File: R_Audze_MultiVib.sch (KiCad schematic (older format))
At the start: 11 parts

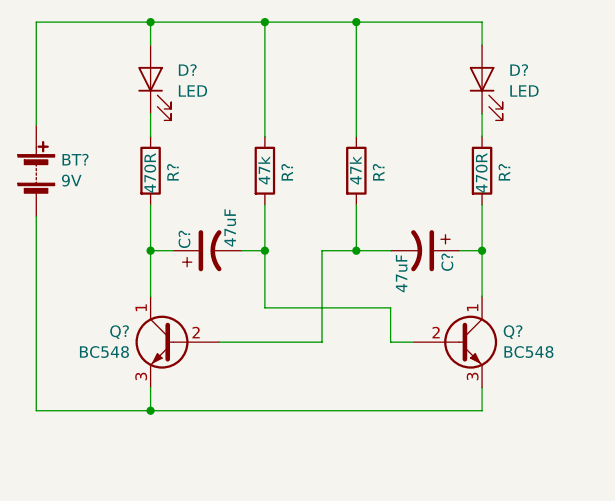
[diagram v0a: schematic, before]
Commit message: Replaced transistors with a double unit IC
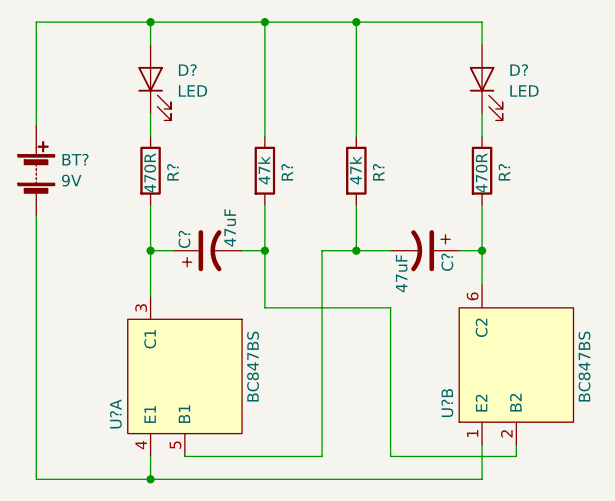
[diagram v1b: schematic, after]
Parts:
- removed Q? (x2): BC548, Package_TO_SOT_THT:TO-92_Inline, symbol Transistor_BJT:BC548
- added U? (x2): BC847BS, symbol project_library:BC847BS
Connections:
- net at BT?.2 (-): now also U?.1 (E2), U?.4 (E1)
- net at C?.1, R?.2: now also U?.3 (C1)
- net at C?.2, R?.2: now also U?.2 (B2)
- net at C?.2, R?.2: now also U?.5 (B1)
- net at C?.1, R?.2: now also U?.6 (C2)
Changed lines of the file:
@@
 EESchema Schematic File Version 4
+LIBS:R_Audze_MultiVib-cache
 EELAYER 26 0
 EELAYER END
@@
 $Comp
 L Device:CP1 C?
-U 1 1 5E56251E
-P 3350 4450
-F 0 "C?" H 3400 4550 50  0000 C CNN
-F 1 "47uF" H 3450 4350 50  0000 C CNN
-F 2 "" H 3350 4450 50  0001 C CNN
-F 3 "~" H 3350 4450 50  0001 C CNN
-	1    3350 4450
-	0    -1   -1   0
-$EndComp
-$Comp
-L Device:CP1 C?
 U 1 1 5E562593
 P 4300 4450
@@
 Wire Wire Line
 	4550 3450 4550 3550
-Connection ~ 3600 3450
 Wire Wire Line
 	4550 3950 4550 3850
@@
 Wire Wire Line
 	4000 3450 4550 3450
-$Comp
-L Transistor_BJT:BC548 Q?
-U 1 1 5E562A15
-P 3200 4850
-F 0 "Q?" H 3390 4896 50  0000 L CNN
-F 1 "BC548" H 3390 4805 50  0000 L CNN
-F 2 "Package_TO_SOT_THT:TO-92_Inline" H 3400 4775 50  0001 L CIN
-F 3 "http://www.fairchildsemi.com/ds/BC/BC547.pdf" H 3200 4850 50  0001 L CNN
-	1    3200 4850
-	-1   0    0    -1
-$EndComp
-$Comp
-L Transistor_BJT:BC548 Q?
-U 1 1 5E562A81
-P 4450 4850
-F 0 "Q?" H 4641 4896 50  0000 L CNN
-F 1 "BC548" H 4641 4805 50  0000 L CNN
-F 2 "Package_TO_SOT_THT:TO-92_Inline" H 4650 4775 50  0001 L CIN
-F 3 "http://www.fairchildsemi.com/ds/BC/BC547.pdf" H 4450 4850 50  0001 L CNN
-	1    4450 4850
-	1    0    0    -1
-$EndComp
 Wire Wire Line
 	3100 4450 3100 4650
@@
 Wire Wire Line
 	4000 4450 3850 4450
-Wire Wire Line
-	3850 4450 3850 4850
-Wire Wire Line
-	3850 4850 3400 4850
 Connection ~ 4000 4450
 Wire Wire Line
@@
 Wire Wire Line
 	3600 4700 4150 4700
-Wire Wire Line
-	4150 4700 4150 4850
-Wire Wire Line
-	4150 4850 4250 4850
 Connection ~ 3600 4450
 Wire Wire Line
-	4550 4450 4550 4650
+	4550 4450 4550 4600
 Connection ~ 4550 4450
 Wire Wire Line
@@
 	2600 3450 3100 3450
 Wire Wire Line
-	2600 4300 2600 5150
-Wire Wire Line
-	2600 5150 3100 5150
-Wire Wire Line
-	4550 5150 4550 5050
-Wire Wire Line
-	3100 5050 3100 5150
-Connection ~ 3100 5150
-Wire Wire Line
-	3100 5150 4550 5150
+	2600 4300 2600 5450
+Wire Wire Line
+	2600 5450 3100 5450
+Wire Wire Line
+	4550 5450 4550 5300
+Connection ~ 3100 5450
+Wire Wire Line
+	3100 5450 4550 5450
+Connection ~ 3600 3450
+$Comp
+L Device:CP1 C?
+U 1 1 5E56251E
+P 3350 4450
+F 0 "C?" H 3400 4550 50  0000 C CNN
+F 1 "47uF" H 3450 4350 50  0000 C CNN
+F 2 "" H 3350 4450 50  0001 C CNN
+F 3 "~" H 3350 4450 50  0001 C CNN
+	1    3350 4450
+	0    -1   -1   0
+$EndComp
+$Comp
+L project_library:BC847BS U?
+U 1 1 5E5F7330
+P 3250 5000
+F 0 "U?" H 3350 4700 50  0000 L CNN
+F 1 "BC847BS" H 3050 5300 50  0000 L CNN
+F 2 "" H 3250 4900 50  0001 C CNN
+F 3 "" H 3250 4900 50  0001 C CNN
+	1    3250 5000
+	0    1    1    0
+$EndComp
+$Comp
+L project_library:BC847BS U?
+U 2 1 5E5F737F
+P 4700 4950
+F 0 "U?" H 4600 5250 50  0000 R CNN
+F 1 "BC847BS" H 4850 4650 50  0000 R CNN
+F 2 "" H 4700 4850 50  0001 C CNN
+F 3 "" H 4700 4850 50  0001 C CNN
+	2    4700 4950
+	0    -1   -1   0
+$EndComp
+Wire Wire Line
+	3850 5350 3250 5350
+Wire Wire Line
+	3850 4450 3850 5350
+Wire Wire Line
+	3100 5350 3100 5450
+Wire Wire Line
+	4150 5350 4700 5350
+Wire Wire Line
+	4700 5350 4700 5300
+Wire Wire Line
+	4150 4700 4150 5350
 $EndSCHEMATC

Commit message: Added component annotations
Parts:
- gave numbers to parts that had none: 10
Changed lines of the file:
@@
 $EndDescr
 $Comp
-L Device:Battery BT?
+L Device:Battery BT1
 U 1 1 5E562185
 P 2600 4100
-F 0 "BT?" H 2708 4146 50  0000 L CNN
+F 0 "BT1" H 2708 4146 50  0000 L CNN
 F 1 "9V" H 2708 4055 50  0000 L CNN
 F 2 "" V 2600 4160 50  0001 C CNN
@@
 $EndComp
 $Comp
-L Device:LED D?
+L Device:LED D1
 U 1 1 5E56220C
 P 3100 3700
-F 0 "D?" V 3138 3583 50  0000 R CNN
+F 0 "D1" V 3138 3583 50  0000 R CNN
 F 1 "LED" V 3047 3583 50  0000 R CNN
 F 2 "" H 3100 3700 50  0001 C CNN
@@
 $EndComp
 $Comp
-L Device:LED D?
+L Device:LED D2
 U 1 1 5E56224F
 P 4550 3700
-F 0 "D?" V 4588 3583 50  0000 R CNN
+F 0 "D2" V 4588 3583 50  0000 R CNN
 F 1 "LED" V 4497 3583 50  0000 R CNN
 F 2 "" H 4550 3700 50  0001 C CNN
@@
 $EndComp
 $Comp
-L Device:R R?
+L Device:R R1
 U 1 1 5E562292
 P 3100 4100
-F 0 "R?" V 3200 4050 50  0000 L CNN
+F 0 "R1" V 3200 4050 50  0000 L CNN
 F 1 "470R" V 3100 4000 50  0000 L CNN
 F 2 "" V 3030 4100 50  0001 C CNN
@@
 $EndComp
 $Comp
-L Device:R R?
+L Device:R R2
 U 1 1 5E5622C0
 P 3600 4100
-F 0 "R?" V 3700 4050 50  0000 L CNN
+F 0 "R2" V 3700 4050 50  0000 L CNN
 F 1 "47k" V 3600 4100 50  0000 C CNN
 F 2 "" V 3530 4100 50  0001 C CNN
@@
 $EndComp
 $Comp
-L Device:R R?
+L Device:R R3
 U 1 1 5E5622F0
 P 4000 4100
-F 0 "R?" V 4100 4050 50  0000 L CNN
+F 0 "R3" V 4100 4050 50  0000 L CNN
 F 1 "47k" V 4000 4100 50  0000 C CNN
 F 2 "" V 3930 4100 50  0001 C CNN
@@
 $EndComp
 $Comp
-L Device:R R?
+L Device:R R4
 U 1 1 5E562318
 P 4550 4100
-F 0 "R?" V 4650 4050 50  0000 L CNN
+F 0 "R4" V 4650 4050 50  0000 L CNN
 F 1 "470R" V 4550 4000 50  0000 L CNN
 F 2 "" V 4480 4100 50  0001 C CNN
@@
 $EndComp
 $Comp
-L Device:CP1 C?
+L Device:CP1 C2
 U 1 1 5E562593
 P 4300 4450
-F 0 "C?" H 4350 4550 50  0000 C CNN
+F 0 "C2" H 4350 4550 50  0000 C CNN
 F 1 "47uF" H 4400 4350 50  0000 C CNN
 F 2 "" H 4300 4450 50  0001 C CNN
@@
 Connection ~ 3600 3450
 $Comp
-L Device:CP1 C?
+L Device:CP1 C1
 U 1 1 5E56251E
 P 3350 4450
-F 0 "C?" H 3400 4550 50  0000 C CNN
+F 0 "C1" H 3400 4550 50  0000 C CNN
 F 1 "47uF" H 3450 4350 50  0000 C CNN
 F 2 "" H 3350 4450 50  0001 C CNN
@@
 $EndComp
 $Comp
-L project_library:BC847BS U?
+L project_library:BC847BS U1
 U 1 1 5E5F7330
 P 3250 5000
-F 0 "U?" H 3350 4700 50  0000 L CNN
+F 0 "U1" H 3350 4700 50  0000 L CNN
 F 1 "BC847BS" H 3050 5300 50  0000 L CNN
 F 2 "" H 3250 4900 50  0001 C CNN
@@
 $EndComp
 $Comp
-L project_library:BC847BS U?
+L project_library:BC847BS U1
 U 2 1 5E5F737F
 P 4700 4950
-F 0 "U?" H 4600 5250 50  0000 R CNN
+F 0 "U1" H 4600 5250 50  0000 R CNN
 F 1 "BC847BS" H 4850 4650 50  0000 R CNN
 F 2 "" H 4700 4850 50  0001 C CNN
